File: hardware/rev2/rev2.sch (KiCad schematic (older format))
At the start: 24 parts, among them J1 Conn_01x09_Female, J2 RFM9X_header, J3 Conn_02x03_Odd_Even, U2 MPL3115A2, U3 Teensy3.6, U5 ADXL345BCCZ, U7 TPS2113ADRBR

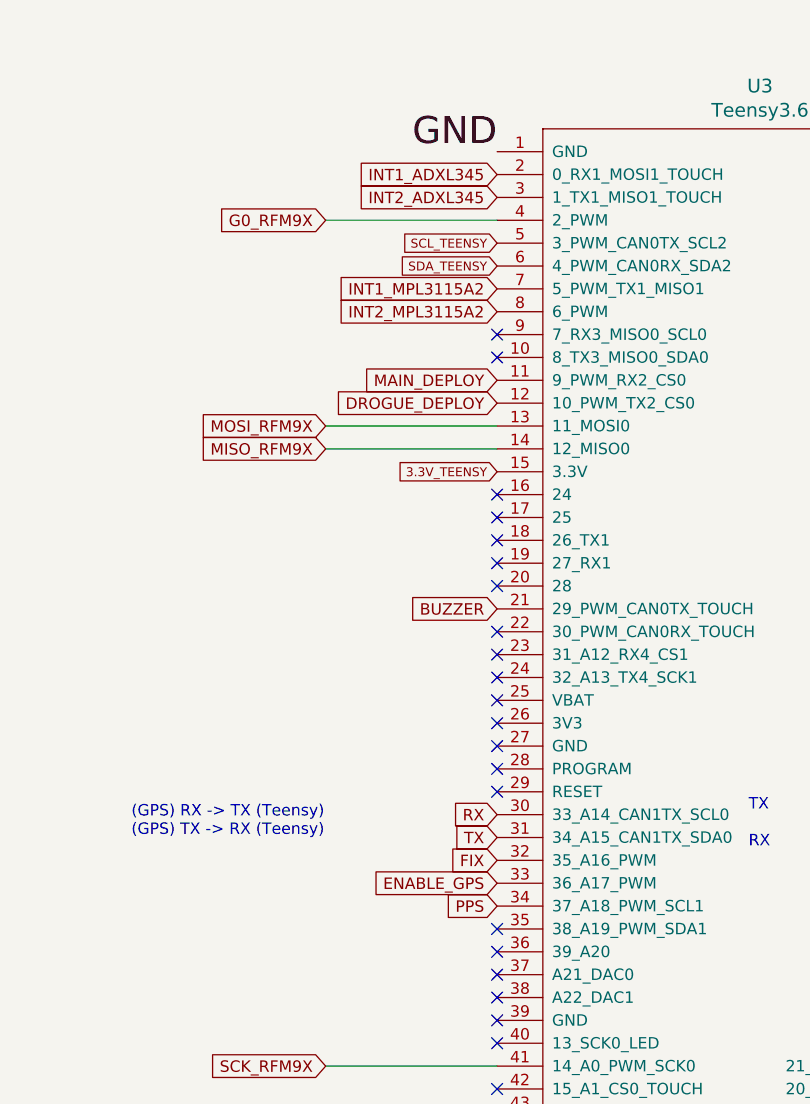
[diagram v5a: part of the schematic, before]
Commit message: significantly change Teensy connections
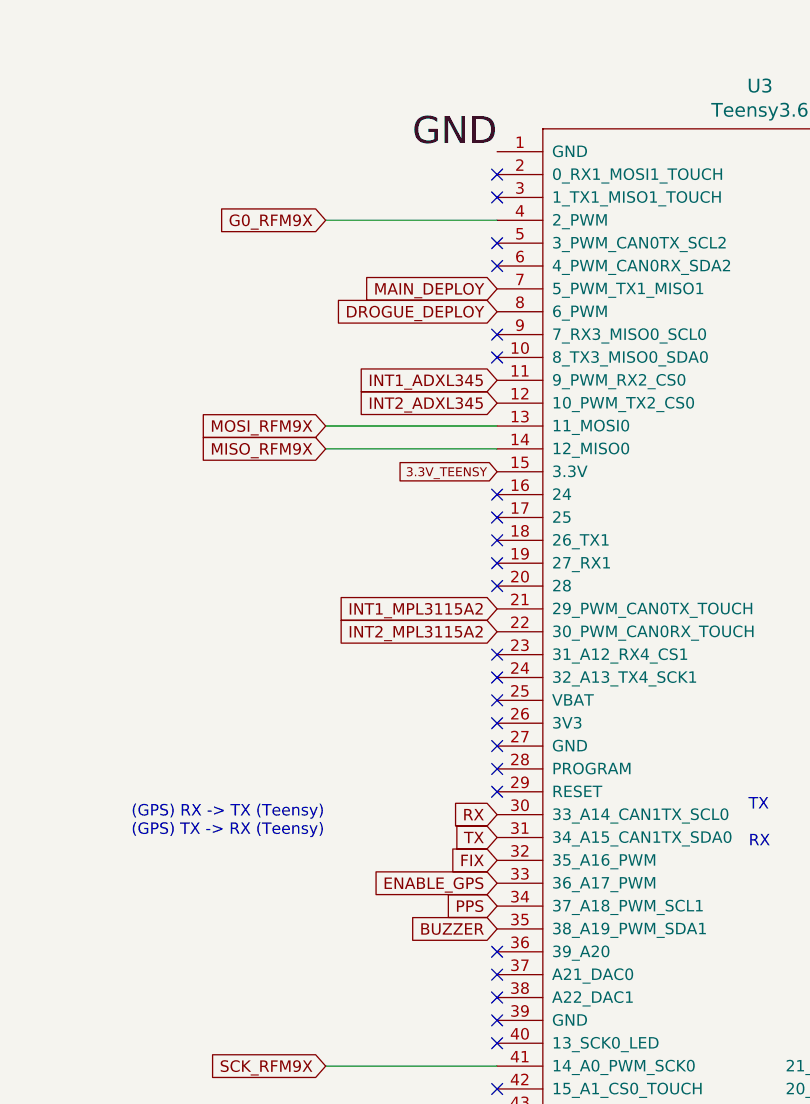
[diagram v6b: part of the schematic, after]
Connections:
- net BUZZER: now also U3.35 (38_A19_PWM_SDA1); no longer U3.21 (29_PWM_CAN0TX_TOUCH)
- net DROGUE_DEPLOY: now also U3.8 (6_PWM); no longer U3.12 (10_PWM_TX2_CS0)
- net INT1_ADXL345: now also U3.11 (9_PWM_RX2_CS0); no longer U3.2 (0_RX1_MOSI1_TOUCH)
- net INT1_MPL3115A2: now also U3.21 (29_PWM_CAN0TX_TOUCH); no longer U3.7 (5_PWM_TX1_MISO1)
- net INT2_ADXL345: now also U3.12 (10_PWM_TX2_CS0); no longer U3.3 (1_TX1_MISO1_TOUCH)
- net INT2_MPL3115A2: now also U3.22 (30_PWM_CAN0RX_TOUCH); no longer U3.8 (6_PWM)
- net MAIN_DEPLOY: now also U3.7 (5_PWM_TX1_MISO1); no longer U3.11 (9_PWM_RX2_CS0)
- net SCL_TEENSY: no longer U3.5 (3_PWM_CAN0TX_SCL2)
- net SDA_TEENSY: no longer U3.6 (4_PWM_CAN0RX_SDA2)
- no-connect marks 72 -> 74
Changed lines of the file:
@@
 Text Label 27650 6500 2    118  ~ 0
 GND
-Text GLabel 27650 7100 0    50   Input ~ 0
+Text GLabel 27650 8500 0    50   Input ~ 0
 INT1_MPL3115A2
-Text GLabel 27650 7200 0    50   Input ~ 0
+Text GLabel 27650 8600 0    50   Input ~ 0
 INT2_MPL3115A2
 $Comp
@@
 Wire Wire Line
 	10200 12350 10200 12500
-Text GLabel 27650 6900 0    39   Input ~ 0
-SCL_TEENSY
-Text GLabel 27650 7000 0    39   Input ~ 0
-SDA_TEENSY
 NoConn ~ 27650 8400
 NoConn ~ 27650 8900
@@
 Text Notes 3200 14450 0    50   ~ 0
 tantalum capacitor preferred\nsee datasheet page 28.
-Text GLabel 27650 6600 0    50   Input ~ 0
+Text GLabel 27650 7500 0    50   Input ~ 0
 INT1_ADXL345
-Text GLabel 27650 6700 0    50   Input ~ 0
+Text GLabel 27650 7600 0    50   Input ~ 0
 INT2_ADXL345
 Text GLabel 27650 9400 0    50   Input ~ 0
@@
 Text GLabel 29950 10000 2    50   Input ~ 0
 BMS_to_Teensy
-NoConn ~ 27650 9900
 Text Notes 18800 10200 0    250  ~ 0
 <HEADER PINS>
@@
 NoConn ~ 27650 8200
 NoConn ~ 27650 8300
-NoConn ~ 27650 8600
 NoConn ~ 27650 8700
 NoConn ~ 27650 8800
-NoConn ~ 27650 7400
-NoConn ~ 27650 7300
 $Comp
 L power:PWR_FLAG #FLG0101
@@
 	10850 19750 10850 19600
 Connection ~ 10850 19750
-Text GLabel 27650 7500 0    50   Input ~ 0
-MAIN_DEPLOY
-Text GLabel 27650 7600 0    50   Input ~ 0
-DROGUE_DEPLOY
 Text GLabel 11200 21200 2    50   Input ~ 0
 MAIN_DEPLOY
@@
 Wire Wire Line
 	23550 20300 23550 20650
-Text GLabel 27650 8500 0    50   Input ~ 0
+Text GLabel 27650 9900 0    50   Input ~ 0
 BUZZER
+NoConn ~ 27650 7300
+NoConn ~ 27650 7400
+Text GLabel 27650 7200 0    50   Input ~ 0
+DROGUE_DEPLOY
+Text GLabel 27650 7100 0    50   Input ~ 0
+MAIN_DEPLOY
+NoConn ~ 27650 7000
+NoConn ~ 27650 6900
+NoConn ~ 27650 6700
+NoConn ~ 27650 6600
 $EndSCHEMATC

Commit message: add zener diode overvoltage protection, add 10 uF capacitor to radio, add LEDS but do not connect
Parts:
- added C?: C_10uF, footprints:C_0805_OEM, symbol preferred_parts:C_10uF
- added D? (x2): LED, symbol Device:LED
- added D?: D_Zener, Package_TO_SOT_SMD:SOT-23, symbol Device:D_Zener
- added R?: R_20, footprints:R_0805_OEM, symbol Device:R
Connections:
- net +3V3: now also C?.1
- net BMS_to_Teensy: now also D?.1 (K), R?.1; no longer C14.1, U7.7 (OUT)
- net GND: now also C?.2, D?.2 (A)
- new net BMS_TO_ZENER: C14.1, R?.2, U7.7 (OUT)
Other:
- note added: "Needs to be connected to "pins" 1 and 3 on the footprint"
- moved on the sheet: C14, J3, R5, R6, R7, U7

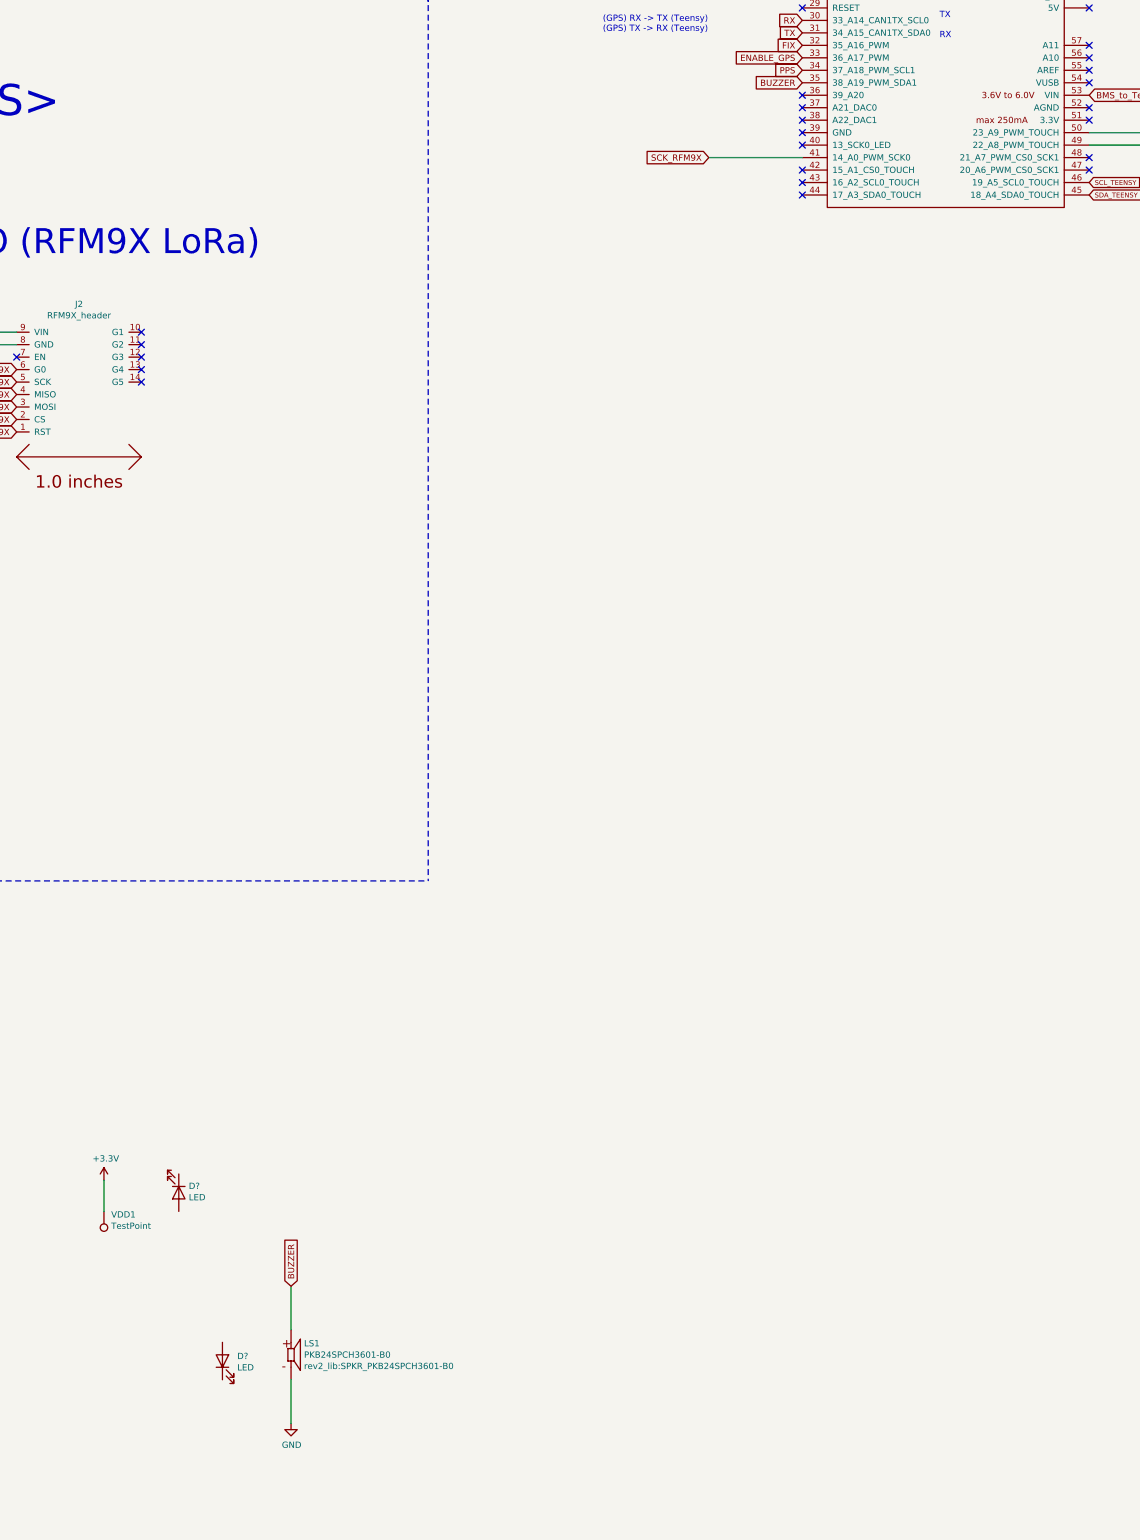
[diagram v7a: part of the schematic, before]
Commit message: add debugging LEDs (may need to change)
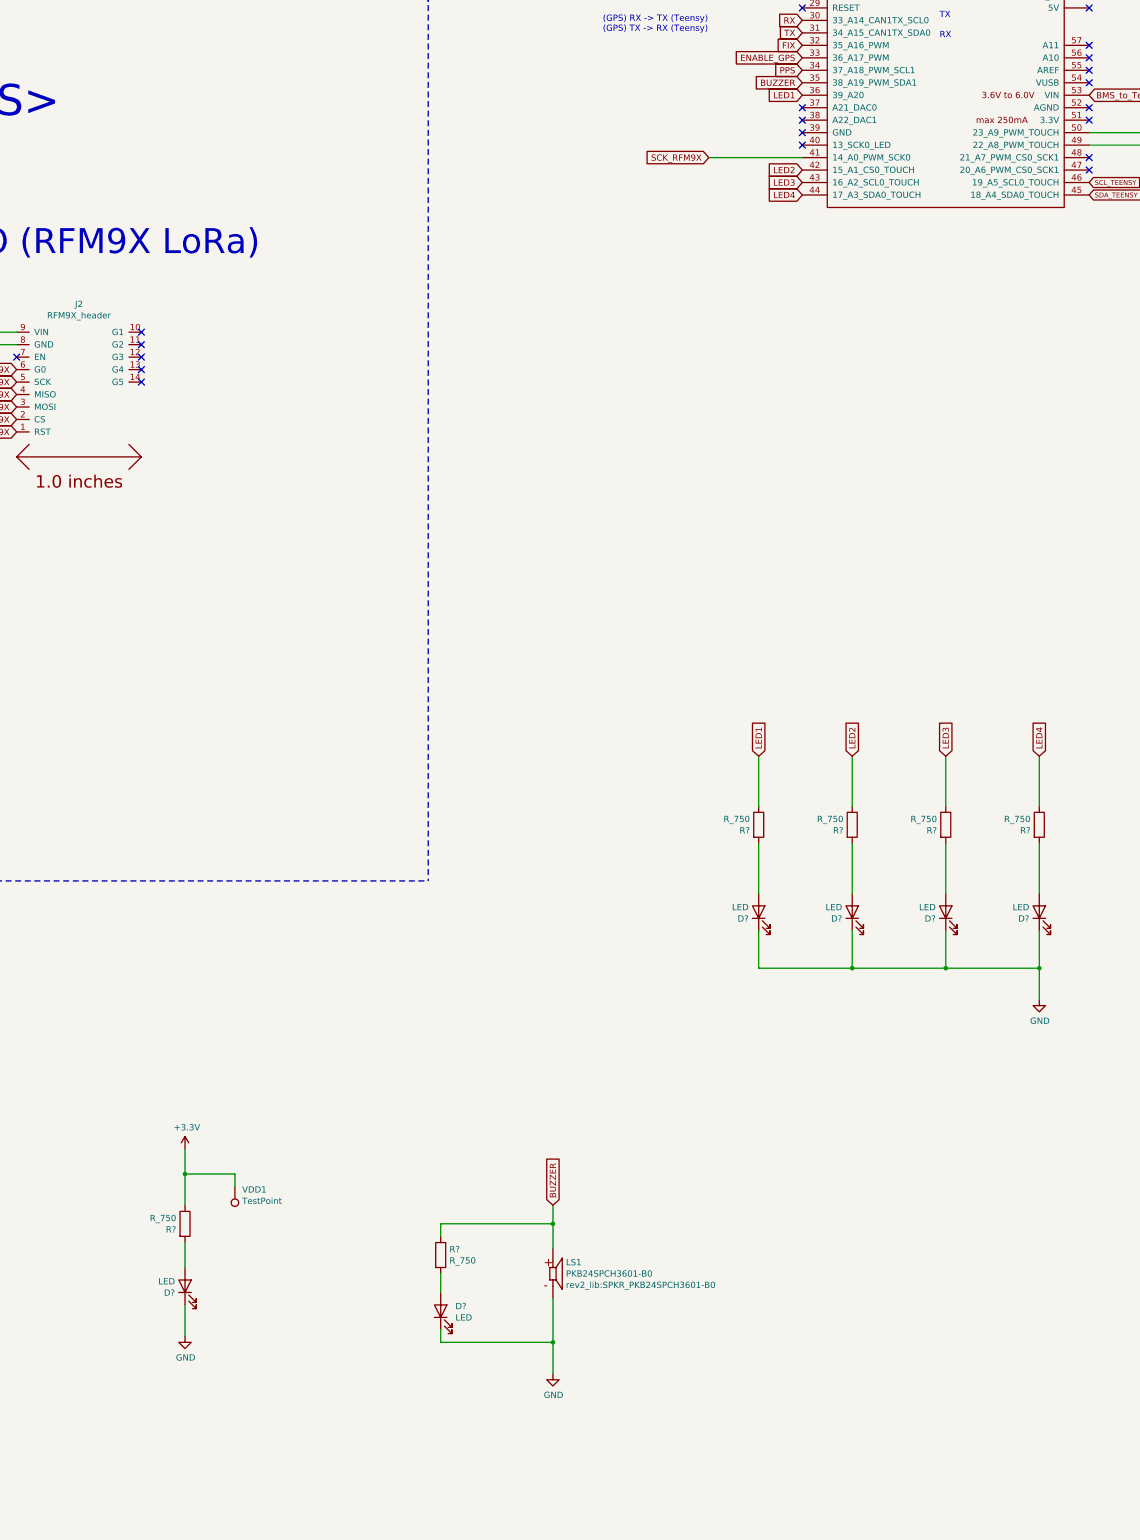
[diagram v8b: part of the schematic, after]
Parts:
- added D? (x4): LED, symbol Device:LED
- added R? (x6): R_750, symbol Device:R
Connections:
- net +3V3: now also R?.1
- net BUZZER: now also R?.1
- net GND: now also D?.1 (K), D?.1 (K), D?.1 (K), D?.1 (K), D?.1 (K), D?.1 (K)
- net at D?.2 (A): now also R?.2 (x2)
- net LED1: now reaches U3.36 (39_A20)
- net LED1: now also R?.1
- net LED2: now reaches U3.42 (15_A1_CS0_TOUCH)
- net LED2: now also R?.1
- net LED3: now reaches U3.43 (16_A2_SCL0_TOUCH)
- net LED3: now also R?.1
- net LED4: now reaches U3.44 (17_A3_SDA0_TOUCH)
- net LED4: now also R?.1
- new net: D?.2 (A), R?.2 (x4)
- no-connect marks 74 -> 70
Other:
- moved on the sheet: D?, LS1, VDD1
